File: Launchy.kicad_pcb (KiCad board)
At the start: 2 copper layers, 61.5 x 50.5 mm, 38 parts, among them IC1 ESP32-C3-MINI-1-N4, IC2 SBC846BPDW1T3G, J1 Conn_02x06_Odd_Even, J2 Conn_01x02, J3 Conn_01x01_Socket, J4 Conn_01x01_Socket, J5 Screw_Terminal_01x03, J6 USB_C_Receptacle_USB2.0_16P, K1 SRD-03VDC-SL-C, Q1 IRLML0030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

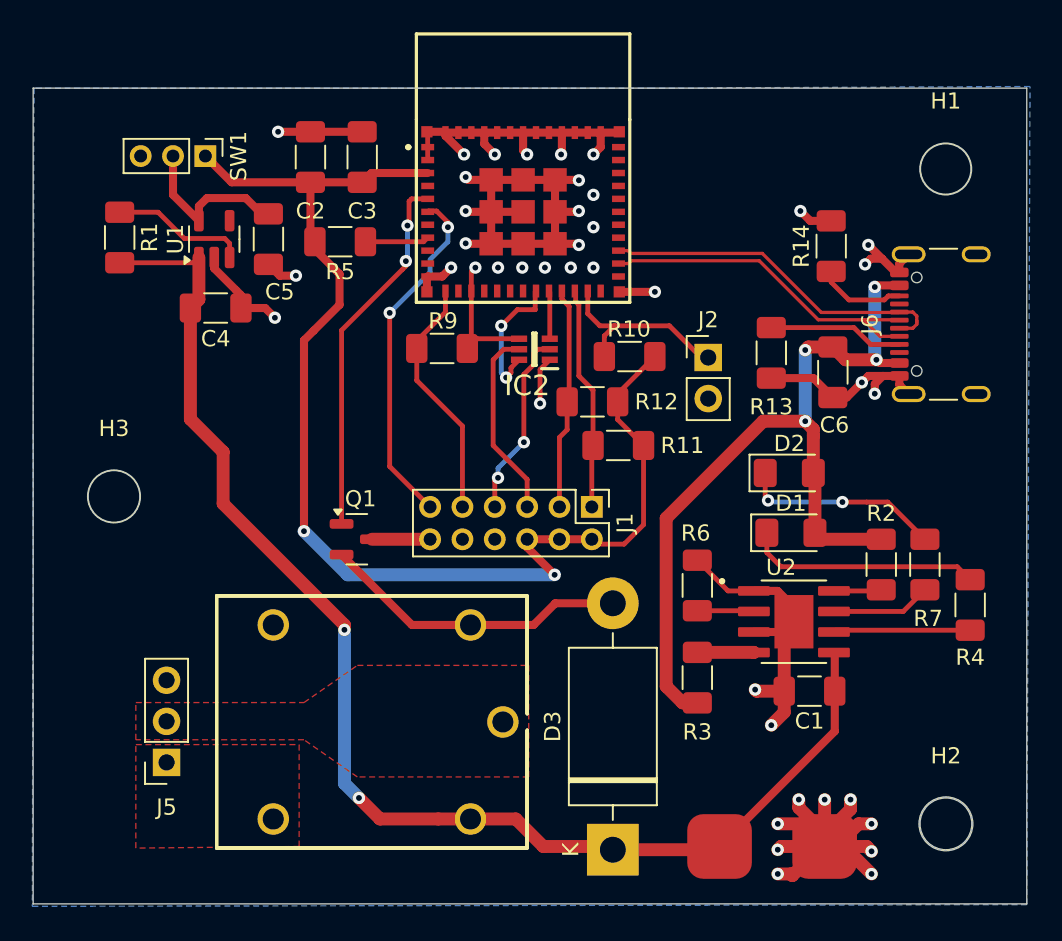
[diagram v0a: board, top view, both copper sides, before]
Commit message: Quality of life changes in Code Symbol and footprint libraries include Schematic and pcb updates, unnecessary dual bjt remove, replacing 2.00mm headers with more common 2.54mm ones Copper Pour tweaks Adding Display demo
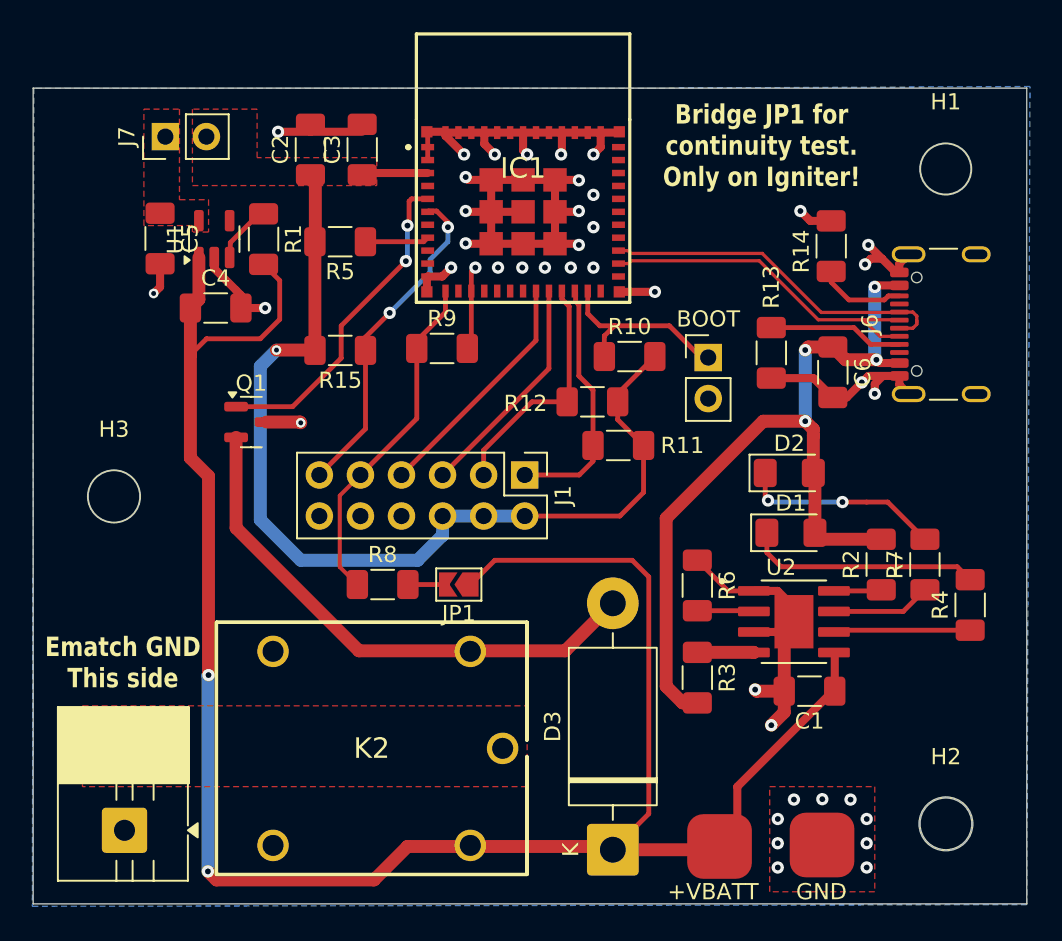
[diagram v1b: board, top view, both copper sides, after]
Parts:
- removed IC2: SBC846BPDW1T3G, SamacSys_Parts:SOT65P210X110-6N
- removed K1: SRD-03VDC-SL-C, SamacSys_Parts:SRD03VDCSLC
- removed SW1: SW_SPDT, Connector_PinHeader_2.00mm:PinHeader_1x03_P2.00mm_Vertical
- added G***: LOGO, Library:logoInverted, F.Cu at (158.5, 70.0)
- added J7: Conn_01x02, Library:PinHeader_1x02_P2.54mm_Vertical, F.Cu at (116.1, 41.3)
- added JP1: SolderJumper_2_Open, Library:SolderJumper-2_P1.3mm_Open_TrianglePad1.0x1.5mm, F.Cu at (134.3, 69.0)
- added K2: SRD-03VDC-SL-C, Library:SRD03VDCSLC, F.Cu at (135.0, 73.1)
- added R15: 10k, Library:C_1206_3216Metric_Pad1.33x1.80mm_HandSolder, F.Cu at (126.9, 54.5)
- added R8: 10k, Library:C_1206_3216Metric_Pad1.33x1.80mm_HandSolder, F.Cu at (129.6, 69.0)
- +VBATT: renamed from J3; footprint CustomLibrary:SolderWirePad_1x01_SMD_4x4mm -> Library:SolderWirePad_1x01_SMD_4x4mm
- BOOT: renamed from J2; footprint Connector_PinHeader_2.54mm:PinHeader_1x02_P2.54mm_Vertical -> Library:PinHeader_1x02_P2.54mm_Vertical
- C1, C2, C3, C4, C5, C6, R1, R10, R11, R12, R13, R14, R2, R3, R4, R5, R6, R7: footprint Capacitor_SMD:C_1206_3216Metric_Pad1.33x1.80mm_HandSolder -> Library:C_1206_3216Metric_Pad1.33x1.80mm_HandSolder
- D1, D2: footprint LED_SMD:LED_1206_3216Metric_Pad1.42x1.75mm_HandSolder -> Library:LED_1206_3216Metric_Pad1.42x1.75mm_HandSolder
- D3: footprint Diode_THT:D_DO-201AD_P15.24mm_Horizontal -> Library:D_DO-201AD_P15.24mm_Horizontal
- GND: renamed from J4; footprint CustomLibrary:SolderWirePad_1x01_SMD_4x4mm -> Library:SolderWirePad_1x01_SMD_4x4mm
- H1, H2, H3: footprint MountingHole:MountingHole_3.2mm_M3 -> Library:MountingHole_3.2mm_M3
- IC1: footprint SamacSys_Parts:ESP32C3MINI1N4 -> Library:ESP32C3MINI1N4
- J1: footprint Connector_PinHeader_2.00mm:PinHeader_2x06_P2.00mm_Vertical -> Library:PinHeader_2x06_P2.54mm_Vertical
- J5: value Screw_Terminal_01x03 -> Screw_Terminal_01x02; footprint Connector_PinSocket_2.54mm:PinSocket_1x03_P2.54mm_Vertical -> Library:TerminalBlock_MaiXu_MX126-5.0-02P_1x02_P5.00mm
- J6: footprint Connector_USB:USB_C_Receptacle_GCT_USB4105-xx-A_16P_TopMnt_Horizontal -> Library:USB_C_Receptacle_GCT_USB4105-xx-A_16P_TopMnt_Horizontal
- Q1: footprint Package_TO_SOT_SMD:SOT-23 -> Library:SOT-23
- R9: value 10k -> 22k; footprint Capacitor_SMD:C_1206_3216Metric_Pad1.33x1.80mm_HandSolder -> Library:C_1206_3216Metric_Pad1.33x1.80mm_HandSolder
- U1: footprint Package_TO_SOT_SMD:SOT-23-5 -> Library:SOT-23-5
- U2: footprint CustomLibrary:SOP127P600X175-9N -> Library:SOP127P600X175-9N
- moved Q1 9.75 mm to (121.4, 59.0)
- moved R1 8.90 mm to (122.2, 47.6)
- moved C5 6.70 mm to (115.8, 47.6)
- moved J5 4.94 mm to (113.6, 84.2), turned to 90 degrees
- moved J1 4.60 mm to (138.3, 62.2)
- moved C2 0.46 mm to (125.1, 42.1)
- moved C3 0.46 mm to (128.3, 42.1)
- moved GND 0.19 mm to (156.7, 85.1)
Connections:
- IC1 pad 19: /GREEN_LED -> /G_LED
- IC1 pad 20: /RED_LED -> /R_LED
- J1 pad 5: /R_BASE -> /R_LED
- J1 pad 7: /G_BASE -> /G_LED
- J5 pad 1: Net-(J5-Pin_1) -> unconnected-(J5-Pin_1-Pad1)
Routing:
- net VBATT+: track 82.0 -> 127.0 mm
- net GND: track 150.6 -> 111.7 mm
- net /G_LED: track 0.00 -> 14.9 mm
- net /R_LED: track 0.00 -> 14.2 mm
- net Net-(D3-A): track 19.1 -> 33.3 mm
- net /R_BASE: track 11.8 -> 0.00 mm
- net /G_BASE: track 11.6 -> 0.00 mm, vias 2 -> 0
- net +3.3V: track 77.3 -> 66.4 mm, vias 2 -> 1
- net Net-(J7-Pin_1): track 10.5 -> 0.00 mm
- net /GREEN_LED: track 8.44 -> 0.00 mm, vias 2 -> 0
- net /PUSH: track 15.3 -> 21.3 mm
- net Net-(U1-EN): track 8.47 -> 3.73 mm
- net /RED_LED: track 2.97 -> 0.00 mm
- net /Relay: track 22.9 -> 20.4 mm
- net Net-(JP1-B): track 0.00 -> 2.43 mm
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- added copper zone on F.Cu, net +3.3V
- added copper zone on F.Cu, net GND
- added copper zone on F.Cu, net Net-(J7-Pin_1)
- removed copper zone on F.Cu, net Net-(J5-Pin_1)
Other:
- board text added: "Bridge JP1 for continuity test. Only on Igniter!"
- board text added: "Ematch GND This side"
